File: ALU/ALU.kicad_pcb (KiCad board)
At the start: 2 copper layers, 99.6 x 59.9 mm, 40 parts, among them J1 Conn_01x16, J2 Conn_01x16, J3 Conn_01x08, J4 Conn_01x08, U1 74LS86, U10 74LS157, U11 74LS08, U12 74LS157, U13 74LS04, U2 74LS86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

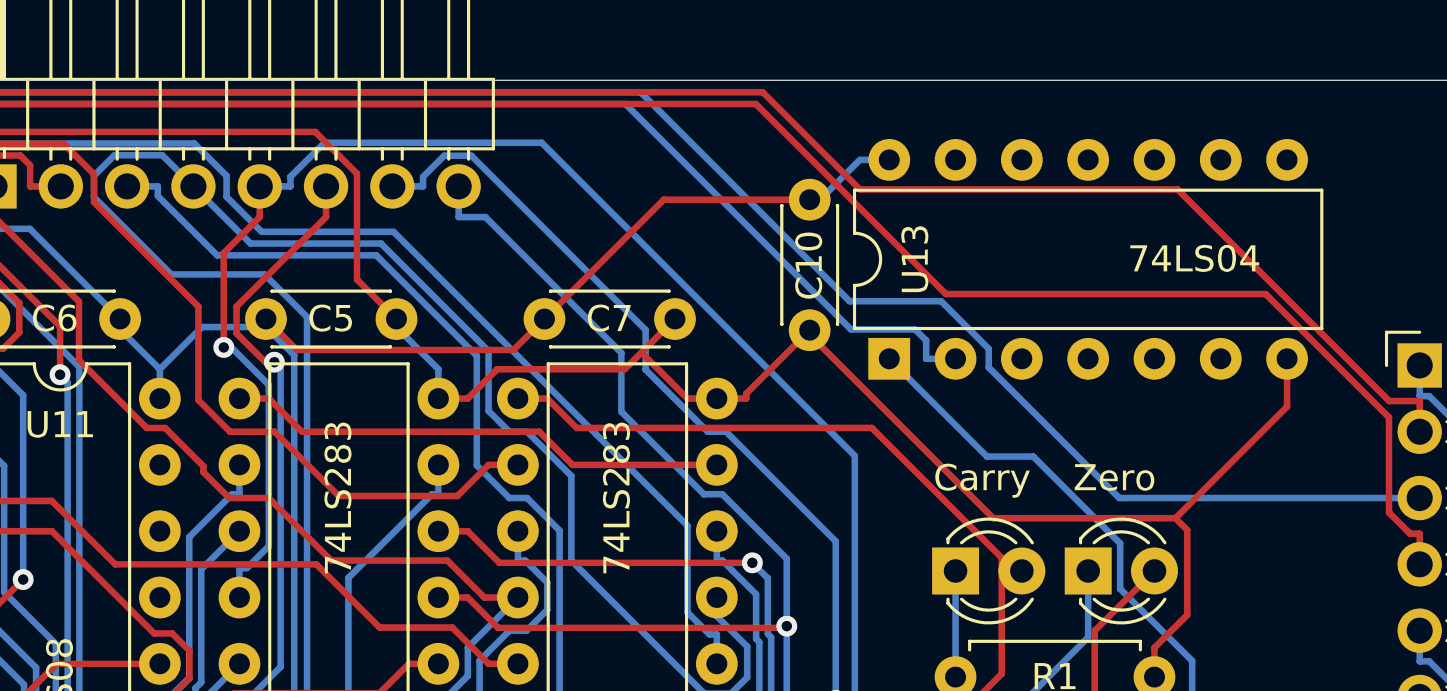
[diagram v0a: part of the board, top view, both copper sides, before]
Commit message: Fixed floating inputs; improved power; added parts list; replaced JK latches
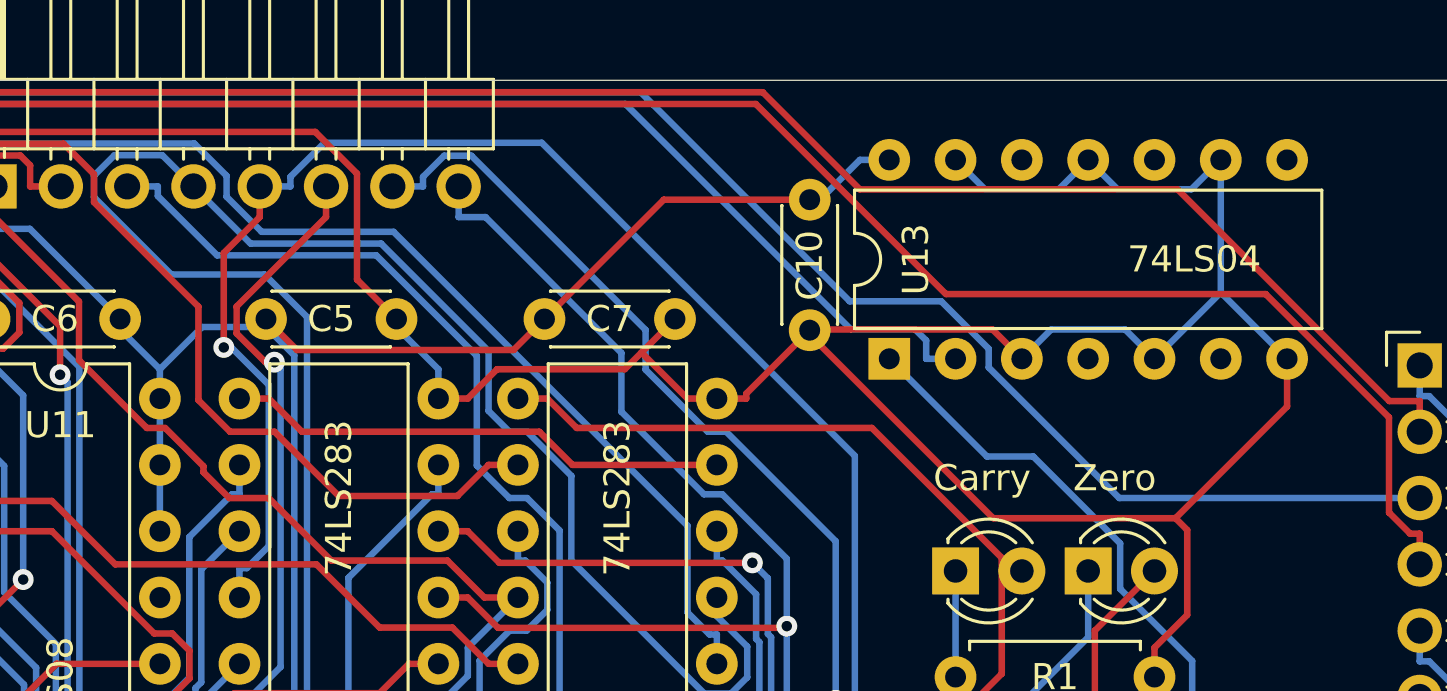
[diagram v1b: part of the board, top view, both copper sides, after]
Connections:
- U11 pad 11: (no net) -> Net-(U11-Pad11)
- U11 pad 12: (no net) -> VCC
- U11 pad 13: (no net) -> VCC
- U13 pad 10: (no net) -> Net-(U13-Pad10)
- U13 pad 11: (no net) -> GND
- U13 pad 12: (no net) -> Net-(U13-Pad12)
- U13 pad 13: (no net) -> GND
- U13 pad 3: (no net) -> GND
- U13 pad 4: (no net) -> Net-(U13-Pad4)
- U13 pad 5: (no net) -> GND
- U13 pad 6: (no net) -> Net-(U13-Pad6)
- U13 pad 8: (no net) -> Net-(U13-Pad8)
- U13 pad 9: (no net) -> GND
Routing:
- net GND: track 325.2 -> 364.1 mm
- net VCC: track 293.7 -> 298.7 mm
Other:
- rule pad_to_mask_clearance: 0.051 -> 0
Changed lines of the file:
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@@
     (thickness 1.6)
     (drawings 8)
-    (tracks 1520)
+    (tracks 1537)
     (zones 0)
     (modules 40)
-    (nets 89)
+    (nets 95)
   )
   (page A4)
@@
     (pad_size 1.524 1.524)
     (pad_drill 0.762)
-    (pad_to_mask_clearance 0.051)
-    (solder_mask_min_width 0.25)
+    (pad_to_mask_clearance 0)
     (aux_axis_origin 0 0)
     (visible_elements FFFFFF7F)
     (pcbplotparams
       (layerselection 0x010fc_ffffffff)
-      (usegerberextensions false)
-      (usegerberattributes false)
+      (usegerberextensions true)
+      (usegerberattributes true)
       (usegerberadvancedattributes false)
-      (creategerberjobfile false)
+      (creategerberjobfile true)
       (excludeedgelayer true)
       (linewidth 0.100000)
@@
       (outputformat 1)
       (mirror false)
-      (drillshape 1)
+      (drillshape 0)
       (scaleselection 1)
-      (outputdirectory ""))
+      (outputdirectory "ALU Gerber/"))
   )
   (net 0 "")
@@
   (net 87 "Net-(U13-Pad2)")
   (net 88 "Net-(U11-Pad10)")
+  (net 89 "Net-(U11-Pad11)")
+  (net 90 "Net-(U13-Pad6)")
+  (net 91 "Net-(U13-Pad12)")
+  (net 92 "Net-(U13-Pad4)")
+  (net 93 "Net-(U13-Pad10)")
+  (net 94 "Net-(U13-Pad8)")
   (net_class Default "This is the default net class."
     (clearance 0.2)
@@
     (add_net "Net-(U11-Pad1)")
     (add_net "Net-(U11-Pad10)")
+    (add_net "Net-(U11-Pad11)")
     (add_net "Net-(U11-Pad2)")
     (add_net "Net-(U11-Pad3)")
@@
     (add_net "Net-(U12-Pad2)")
     (add_net "Net-(U12-Pad5)")
+    (add_net "Net-(U13-Pad10)")
+    (add_net "Net-(U13-Pad12)")
     (add_net "Net-(U13-Pad2)")
+    (add_net "Net-(U13-Pad4)")
+    (add_net "Net-(U13-Pad6)")
+    (add_net "Net-(U13-Pad8)")
     (add_net "Net-(U2-Pad11)")
     (add_net "Net-(U2-Pad3)")
@@
     (pad 7 thru_hole oval (at 0 15.24 90) (size 1.6 1.6) (drill 0.8) (layers *.Cu *.Mask)
       (net 36 GND))
-    (pad 13 thru_hole oval (at 7.62 2.54 90) (size 1.6 1.6) (drill 0.8) (layers *.Cu *.Mask))
-    (pad 6 thru_hole oval (at 0 12.7 90) (size 1.6 1.6) (drill 0.8) (layers *.Cu *.Mask))
-    (pad 12 thru_hole oval (at 7.62 5.08 90) (size 1.6 1.6) (drill 0.8) (layers *.Cu *.Mask))
-    (pad 5 thru_hole oval (at 0 10.16 90) (size 1.6 1.6) (drill 0.8) (layers *.Cu *.Mask))
-    (pad 11 thru_hole oval (at 7.62 7.62 90) (size 1.6 1.6) (drill 0.8) (layers *.Cu *.Mask))
-    (pad 4 thru_hole oval (at 0 7.62 90) (size 1.6 1.6) (drill 0.8) (layers *.Cu *.Mask))
-    (pad 10 thru_hole oval (at 7.62 10.16 90) (size 1.6 1.6) (drill 0.8) (layers *.Cu *.Mask))
-    (pad 3 thru_hole oval (at 0 5.08 90) (size 1.6 1.6) (drill 0.8) (layers *.Cu *.Mask))
-    (pad 9 thru_hole oval (at 7.62 12.7 90) (size 1.6 1.6) (drill 0.8) (layers *.Cu *.Mask))
+    (pad 13 thru_hole oval (at 7.62 2.54 90) (size 1.6 1.6) (drill 0.8) (layers *.Cu *.Mask)
+      (net 36 GND))
+    (pad 6 thru_hole oval (at 0 12.7 90) (size 1.6 1.6) (drill 0.8) (layers *.Cu *.Mask)
+      (net 90 "Net-(U13-Pad6)"))
+    (pad 12 thru_hole oval (at 7.62 5.08 90) (size 1.6 1.6) (drill 0.8) (layers *.Cu *.Mask)
+      (net 91 "Net-(U13-Pad12)"))
+    (pad 5 thru_hole oval (at 0 10.16 90) (size 1.6 1.6) (drill 0.8) (layers *.Cu *.Mask)
+      (net 36 GND))
+    (pad 11 thru_hole oval (at 7.62 7.62 90) (size 1.6 1.6) (drill 0.8) (layers *.Cu *.Mask)
+      (net 36 GND))
+    (pad 4 thru_hole oval (at 0 7.62 90) (size 1.6 1.6) (drill 0.8) (layers *.Cu *.Mask)
+      (net 92 "Net-(U13-Pad4)"))
+    (pad 10 thru_hole oval (at 7.62 10.16 90) (size 1.6 1.6) (drill 0.8) (layers *.Cu *.Mask)
+      (net 93 "Net-(U13-Pad10)"))
+    (pad 3 thru_hole oval (at 0 5.08 90) (size 1.6 1.6) (drill 0.8) (layers *.Cu *.Mask)
+      (net 36 GND))
+    (pad 9 thru_hole oval (at 7.62 12.7 90) (size 1.6 1.6) (drill 0.8) (layers *.Cu *.Mask)
+      (net 36 GND))
     (pad 2 thru_hole oval (at 0 2.54 90) (size 1.6 1.6) (drill 0.8) (layers *.Cu *.Mask)
       (net 87 "Net-(U13-Pad2)"))
-    (pad 8 thru_hole oval (at 7.62 15.24 90) (size 1.6 1.6) (drill 0.8) (layers *.Cu *.Mask))
+    (pad 8 thru_hole oval (at 7.62 15.24 90) (size 1.6 1.6) (drill 0.8) (layers *.Cu *.Mask)
+      (net 94 "Net-(U13-Pad8)"))
     (pad 1 thru_hole rect (at 0 0 90) (size 1.6 1.6) (drill 0.8) (layers *.Cu *.Mask)
       (net 32 SIG_OUT))
@@
     (pad 7 thru_hole oval (at 0 15.24) (size 1.6 1.6) (drill 0.8) (layers *.Cu *.Mask)
       (net 36 GND))
-    (pad 13 thru_hole oval (at 7.62 2.54) (size 1.6 1.6) (drill 0.8) (layers *.Cu *.Mask))
+    (pad 13 thru_hole oval (at 7.62 2.54) (size 1.6 1.6) (drill 0.8) (layers *.Cu *.Mask)
+      (net 35 VCC))
     (pad 6 thru_hole oval (at 0 12.7) (size 1.6 1.6) (drill 0.8) (layers *.Cu *.Mask)
       (net 88 "Net-(U11-Pad10)"))
-    (pad 12 thru_hole oval (at 7.62 5.08) (size 1.6 1.6) (drill 0.8) (layers *.Cu *.Mask))
+    (pad 12 thru_hole oval (at 7.62 5.08) (size 1.6 1.6) (drill 0.8) (layers *.Cu *.Mask)
+      (net 35 VCC))
     (pad 5 thru_hole oval (at 0 10.16) (size 1.6 1.6) (drill 0.8) (layers *.Cu *.Mask)
       (net 83 "Net-(U11-Pad5)"))
-    (pad 11 thru_hole oval (at 7.62 7.62) (size 1.6 1.6) (drill 0.8) (layers *.Cu *.Mask))
+    (pad 11 thru_hole oval (at 7.62 7.62) (size 1.6 1.6) (drill 0.8) (layers *.Cu *.Mask)
+      (net 89 "Net-(U11-Pad11)"))
     (pad 4 thru_hole oval (at 0 7.62) (size 1.6 1.6) (drill 0.8) (layers *.Cu *.Mask)
       (net 85 "Net-(U11-Pad4)"))
@@
   (segment (start 35.56 80.518) (end 35.56 79.3427) (width 0.25) (layer B.Cu) (net 35))
   (segment (start 57.404 36.576) (end 58.5293 36.576) (width 0.25) (layer B.Cu) (net 35))
+  (segment (start 78.74 51.308) (end 78.74 48.768) (width 0.25) (layer B.Cu) (net 35))
+  (segment (start 78.74 48.768) (end 78.74 46.228) (width 0.25) (layer B.Cu) (net 35))
   (segment (start 120.904 76.2) (end 122.0293 76.2) (width 0.25) (layer F.Cu) (net 36))
   (segment (start 122.0293 76.2) (end 122.4957 76.6664) (width 0.25) (layer F.Cu) (net 36))
@@
   (segment (start 35.56 83.058) (end 36.7353 83.058) (width 0.25) (layer F.Cu) (net 36))
   (segment (start 49.784 78.232) (end 48.6587 78.232) (width 0.25) (layer F.Cu) (net 36))
+  (segment (start 113.174999 38.209001) (end 114.3 37.084) (width 0.25) (layer B.Cu) (net 36))
+  (segment (start 110.345001 38.209001) (end 113.174999 38.209001) (width 0.25) (layer B.Cu) (net 36))
+  (segment (start 109.22 37.084) (end 110.345001 38.209001) (width 0.25) (layer B.Cu) (net 36))
+  (segment (start 118.254999 38.209001) (end 119.38 37.084) (width 0.25) (layer B.Cu) (net 36))
+  (segment (start 115.425001 38.209001) (end 118.254999 38.209001) (width 0.25) (layer B.Cu) (net 36))
+  (segment (start 114.3 37.084) (end 115.425001 38.209001) (width 0.25) (layer B.Cu) (net 36))
+  (segment (start 119.38 42.164) (end 121.92 44.704) (width 0.25) (layer B.Cu) (net 36))
+  (segment (start 119.38 37.084) (end 119.38 42.164) (width 0.25) (layer B.Cu) (net 36))
+  (segment (start 119.38 42.164) (end 116.84 44.704) (width 0.25) (layer B.Cu) (net 36))
+  (segment (start 112.885001 43.578999) (end 111.76 44.704) (width 0.25) (layer B.Cu) (net 36))
+  (segment (start 115.714999 43.578999) (end 112.885001 43.578999) (width 0.25) (layer B.Cu) (net 36))
+  (segment (start 116.84 44.704) (end 115.714999 43.578999) (width 0.25) (layer B.Cu) (net 36))
+  (segment (start 103.661001 43.578999) (end 103.632 43.608) (width 0.25) (layer F.Cu) (net 36))
+  (segment (start 110.634999 43.578999) (end 103.661001 43.578999) (width 0.25) (layer F.Cu) (net 36))
+  (segment (start 111.76 44.704) (end 110.634999 43.578999) (width 0.25) (layer F.Cu) (net 36))
   (segment (start 85.1 81.1594) (end 83.7107 79.7701) (width 0.25) (layer B.Cu) (net 37))
   (segment (start 83.7107 79.7701) (end 83.7107 70.8306) (width 0.25) (layer B.Cu) (net 37))

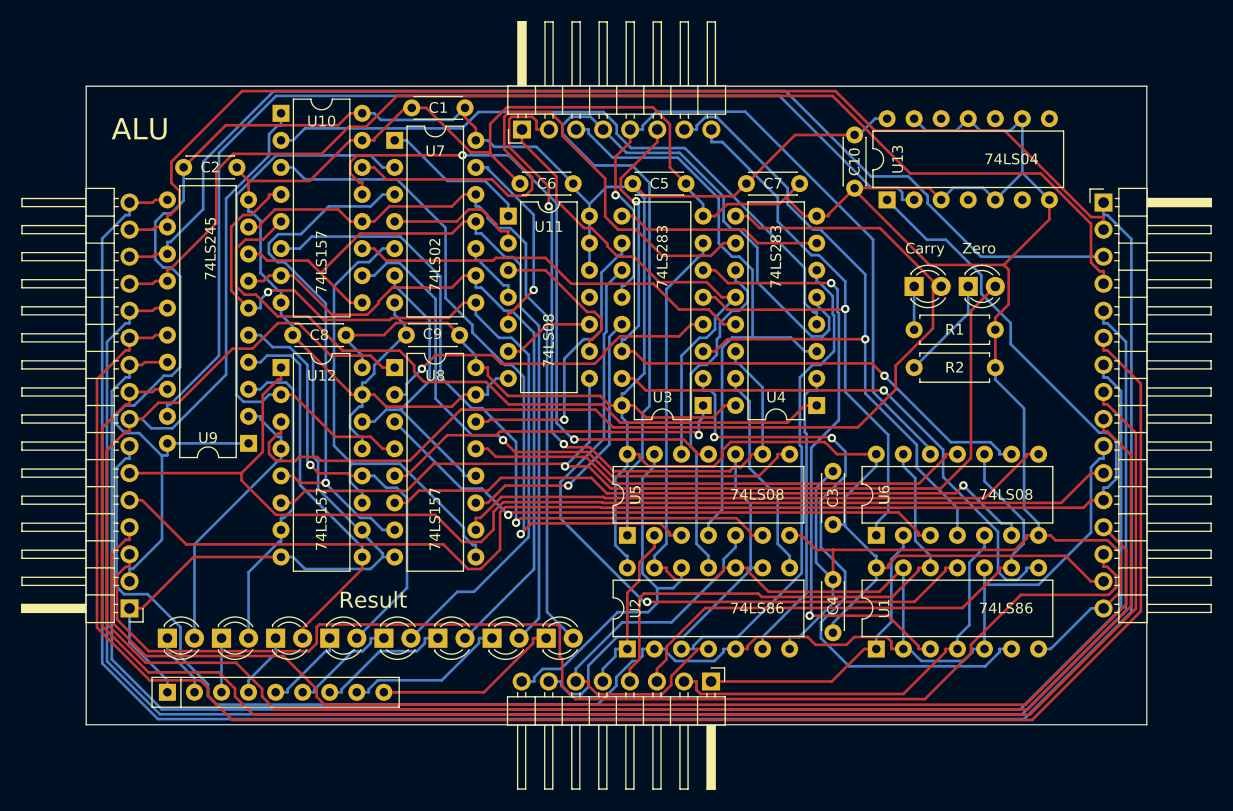
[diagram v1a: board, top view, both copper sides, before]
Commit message: Fix reversed headers on ALU, and counting issues on counter (CET / CEP connections)
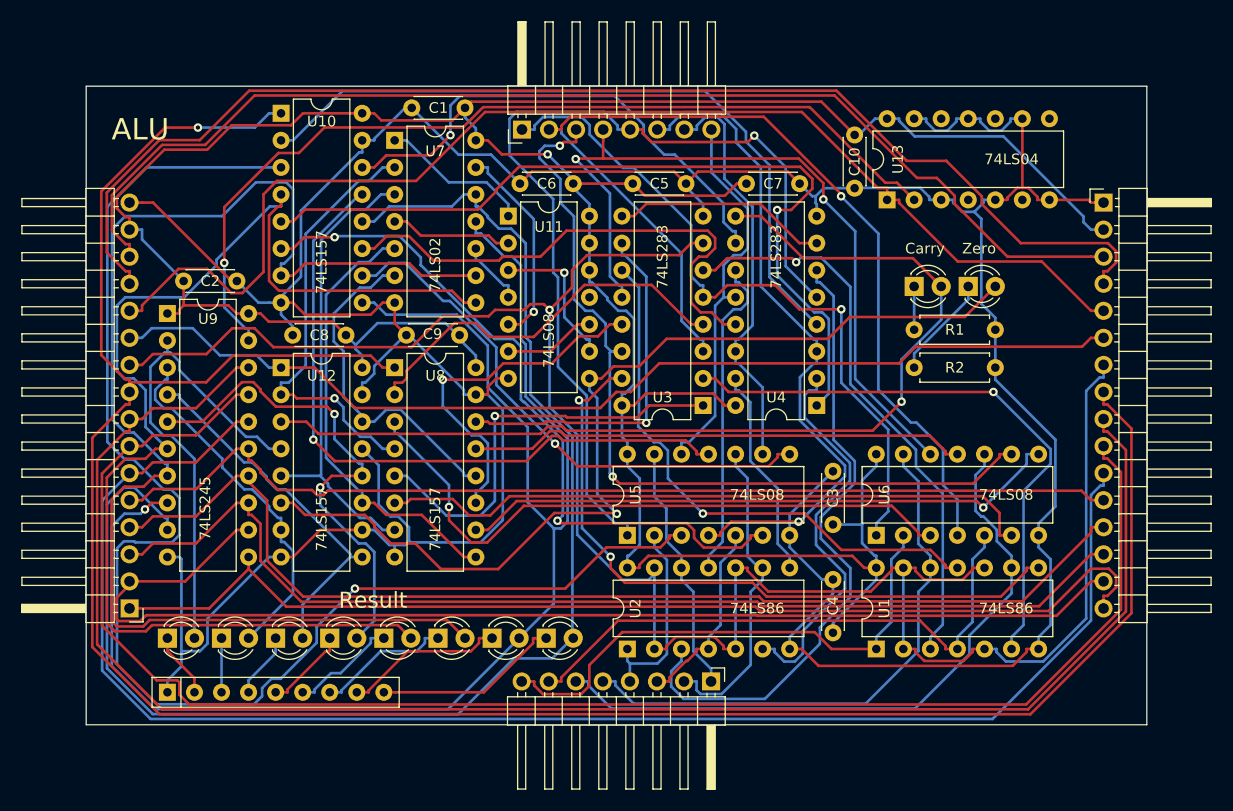
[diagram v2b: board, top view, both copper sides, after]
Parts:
- moved U9 14.4 mm to (39.1, 55.4), turned to 0 degrees
- moved C2 10.7 mm to (40.6, 52.3)
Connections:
- J1 pad 1: GND -> BUS7
- J1 pad 10: BUS1 -> SIG0
- J1 pad 11: BUS2 -> SIG_IN
- J1 pad 12: BUS3 -> SIG_OUT
- J1 pad 13: BUS4 -> CLOCK
- J1 pad 14: BUS5 -> RESET
- J1 pad 15: BUS6 -> VCC
- J1 pad 16: BUS7 -> GND
- J1 pad 2: VCC -> BUS6
- J1 pad 3: RESET -> BUS5
- J1 pad 4: CLOCK -> BUS4
- J1 pad 5: SIG_OUT -> BUS3
- J1 pad 6: SIG_IN -> BUS2
- J1 pad 7: SIG0 -> BUS1
- J1 pad 8: SIG1 -> BUS0
- J1 pad 9: BUS0 -> SIG1
- J2 pad 1: BUS7 -> GND
- J2 pad 10: SIG0 -> BUS1
- J2 pad 11: SIG_IN -> BUS2
- J2 pad 12: SIG_OUT -> BUS3
- J2 pad 13: CLOCK -> BUS4
- J2 pad 14: RESET -> BUS5
- J2 pad 15: VCC -> BUS6
- J2 pad 16: GND -> BUS7
- J2 pad 2: BUS6 -> VCC
- J2 pad 3: BUS5 -> RESET
- J2 pad 4: BUS4 -> CLOCK
- J2 pad 5: BUS3 -> SIG_OUT
- J2 pad 6: BUS2 -> SIG_IN
- J2 pad 7: BUS1 -> SIG0
- J2 pad 8: BUS0 -> SIG1
- J2 pad 9: SIG1 -> BUS0
- J3 pad 1: B0 -> B7
- J3 pad 2: B1 -> B6
- J3 pad 3: B2 -> B5
- J3 pad 4: B3 -> B4
- J3 pad 5: B4 -> B3
- J3 pad 6: B5 -> B2
- J3 pad 7: B6 -> B1
- J3 pad 8: B7 -> B0
- J4 pad 1: A7 -> A0
- J4 pad 2: A6 -> A1
- J4 pad 3: A5 -> A2
- J4 pad 4: A4 -> A3
- J4 pad 5: A3 -> A4
- J4 pad 6: A2 -> A5
- J4 pad 7: A1 -> A6
- J4 pad 8: A0 -> A7
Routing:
- net BUS7: track 190.9 -> 102.6 mm
- net BUS3: track 168.6 -> 96.6 mm
- net Net-(D7-Pad2): track 72.2 -> 140.8 mm, vias 0 -> 1
- net Net-(U10-Pad3): track 66.2 -> 132.3 mm
- net Net-(D6-Pad2): track 64.4 -> 124.8 mm
- net Net-(D8-Pad2): track 70.0 -> 130.5 mm
- net Net-(D5-Pad2): track 78.5 -> 115.7 mm, vias 1 -> 0
- net A6: track 69.0 -> 38.9 mm, vias 2 -> 0
- net A1: track 68.5 -> 95.7 mm
- net SIG_OUT: track 138.2 -> 114.2 mm
- net B0: track 28.5 -> 49.9 mm
- net BUS2: track 165.9 -> 145.8 mm
- net B5: track 38.2 -> 18.2 mm
- net Net-(D1-Pad2): track 26.4 -> 45.8 mm
- net Net-(U2-Pad3): track 45.5 -> 60.9 mm
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
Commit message: Update all boards to r3, and update revision log and gitignore
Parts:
- added HOLE1: MountingHole_2.2mm_M2_DIN965_Pad, MountingHole:MountingHole_2.2mm_M2_DIN965_Pad, F.Cu at (35.6, 38.1)
- added HOLE2: MountingHole_2.2mm_M2_DIN965_Pad, MountingHole:MountingHole_2.2mm_M2_DIN965_Pad, F.Cu at (127.0, 38.1)
- added HOLE3: MountingHole_2.2mm_M2_DIN965_Pad, MountingHole:MountingHole_2.2mm_M2_DIN965_Pad, F.Cu at (35.6, 89.9)
- added HOLE4: MountingHole_2.2mm_M2_DIN965_Pad, MountingHole:MountingHole_2.2mm_M2_DIN965_Pad, F.Cu at (127.0, 89.9)
- U1, U2: value 74LS86 -> 74HC86
- U10, U12, U8: value 74LS157 -> 74HC157
- U11, U5, U6: value 74LS08 -> 74HC08
- U13: value 74LS04 -> 74LHC04
- U3, U4: value 74LS283 -> 74HC283
- U7: value 74LS02 -> 74HC02
- U9: value 74LS245 -> 74HC245
- moved RN1 25.9 mm to (65.0, 90.9), turned to 180 degrees
- moved D1 0.76 mm to (39.9, 85.9)
- moved D2 0.76 mm to (45.0, 85.9)
- moved D4 0.76 mm to (55.1, 85.9)
- moved D5 0.76 mm to (60.2, 85.9)
- moved D6 0.76 mm to (65.3, 85.9)
- moved D7 0.76 mm to (70.4, 85.9)
- moved D8 0.76 mm to (75.4, 85.9)
- moved D3 0.76 mm to (50.0, 85.9)
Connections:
- D1 pad 1: Net-(D1-Pad1) -> Net-(D1-K)
- D1 pad 2: Net-(D1-Pad2) -> Net-(D1-A)
- D2 pad 1: Net-(D2-Pad1) -> Net-(D2-K)
- D2 pad 2: Net-(D2-Pad2) -> Net-(D2-A)
- D3 pad 1: Net-(D3-Pad1) -> Net-(D3-K)
- D3 pad 2: Net-(D3-Pad2) -> Net-(D3-A)
- D4 pad 1: Net-(D4-Pad1) -> Net-(D4-K)
- D4 pad 2: Net-(D4-Pad2) -> Net-(D4-A)
- D5 pad 1: Net-(D5-Pad1) -> Net-(D5-K)
- D5 pad 2: Net-(D5-Pad2) -> Net-(D5-A)
- D6 pad 1: Net-(D6-Pad1) -> Net-(D6-K)
- D6 pad 2: Net-(D6-Pad2) -> Net-(D6-A)
- D7 pad 1: Net-(D7-Pad1) -> Net-(D7-K)
- D7 pad 2: Net-(D7-Pad2) -> Net-(D7-A)
- D8 pad 1: Net-(D8-Pad1) -> Net-(D8-K)
- D8 pad 2: Net-(D8-Pad2) -> Net-(D8-A)
- RN1 pad 2: Net-(D1-Pad1) -> Net-(D8-K)
- RN1 pad 3: Net-(D2-Pad1) -> Net-(D7-K)
- RN1 pad 4: Net-(D3-Pad1) -> Net-(D6-K)
- RN1 pad 5: Net-(D4-Pad1) -> Net-(D5-K)
- RN1 pad 6: Net-(D5-Pad1) -> Net-(D4-K)
- RN1 pad 7: Net-(D6-Pad1) -> Net-(D3-K)
- RN1 pad 8: Net-(D7-Pad1) -> Net-(D2-K)
- RN1 pad 9: Net-(D8-Pad1) -> Net-(D1-K)
- U10 pad 12: Net-(D8-Pad2) -> Net-(D1-A)
- U10 pad 4: Net-(D5-Pad2) -> Net-(D4-A)
- U10 pad 7: Net-(D6-Pad2) -> Net-(D3-A)
- U10 pad 9: Net-(D7-Pad2) -> Net-(D2-A)
- U11 pad 11: Net-(U11-Pad11) -> unconnected-(U11-Pad11)
- U12 pad 12: Net-(D4-Pad2) -> Net-(D5-A)
- U12 pad 4: Net-(D1-Pad2) -> Net-(D8-A)
- U12 pad 7: Net-(D2-Pad2) -> Net-(D7-A)
- U12 pad 9: Net-(D3-Pad2) -> Net-(D6-A)
- U13 pad 10: Net-(U13-Pad10) -> unconnected-(U13-Pad10)
- U13 pad 12: Net-(U13-Pad12) -> unconnected-(U13-Pad12)
- U13 pad 4: Net-(U13-Pad4) -> unconnected-(U13-Pad4)
- U13 pad 6: Net-(U13-Pad6) -> unconnected-(U13-Pad6)
- U13 pad 8: Net-(U13-Pad8) -> unconnected-(U13-Pad8)
- U7 pad 11: Net-(D7-Pad2) -> Net-(D2-A)
- U7 pad 12: Net-(D8-Pad2) -> Net-(D1-A)
- U7 pad 8: Net-(D5-Pad2) -> Net-(D4-A)
- U7 pad 9: Net-(D6-Pad2) -> Net-(D3-A)
- U9 pad 2: Net-(D1-Pad2) -> Net-(D8-A)
- U9 pad 3: Net-(D2-Pad2) -> Net-(D7-A)
- U9 pad 4: Net-(D3-Pad2) -> Net-(D6-A)
- U9 pad 5: Net-(D4-Pad2) -> Net-(D5-A)
- U9 pad 6: Net-(D5-Pad2) -> Net-(D4-A)
- U9 pad 7: Net-(D6-Pad2) -> Net-(D3-A)
- U9 pad 8: Net-(D7-Pad2) -> Net-(D2-A)
- U9 pad 9: Net-(D8-Pad2) -> Net-(D1-A)
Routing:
- net Net-(D7-Pad2): track 140.8 -> 0.00 mm, vias 1 -> 0
- net Net-(D8-Pad2): track 130.5 -> 0.00 mm
- net Net-(D6-Pad2): track 124.8 -> 0.00 mm
- net Net-(D5-Pad2): track 115.7 -> 0.00 mm
- net Net-(D1-A): track 0.00 -> 84.8 mm, vias 0 -> 1
- net Net-(D4-A): track 0.00 -> 83.1 mm, vias 0 -> 1
- net SIG1: track 218.2 -> 139.3 mm
- net SIG_OUT: track 114.2 -> 188.2 mm
- net Net-(D3-A): track 0.00 -> 72.1 mm, vias 0 -> 1
- net Net-(D2-A): track 0.00 -> 69.8 mm, vias 0 -> 4
- net Net-(D8-A): track 0.00 -> 61.9 mm, vias 0 -> 1
- net Net-(U10-I1a): track 132.3 -> 71.4 mm
- net Net-(D5-A): track 0.00 -> 60.2 mm
- net BUS1: track 150.5 -> 99.1 mm, vias 0 -> 1
- net Net-(D7-A): track 0.00 -> 50.2 mm
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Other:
- net class Default removed
